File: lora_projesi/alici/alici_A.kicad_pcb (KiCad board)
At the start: 4 copper layers, 88 x 102 mm, 135 parts, among them J1 USB-C, J2 SMA, J3 RJ45, J4 u.FL (ANA ANTEN), J5 12 V GIRIS, J6 LAMBA, J7 MICRO-SIM, K1 SRD-12VDC-SL-A, Q1 AO3401A, Q2 MMBT2222A, Q3 MMBT2222A, Q4 MMBT2222A, SW1 DUGME, U1 ESP32-S3-WROOM-1-N4, U10 A7670SA, U11 AP2112K-3.3, U12 USBLC6-2SC6, U13 USBLC6-2SC6, U14 USBLC6-2SC6, U15 LM66100, U4 Ra-01H, U5 TPS62933DRLR, U6 TPS62933DRLR, U7 USBLC6-2SC6, U8 TXB0104PW, U9 W5500, Y1 25 MHz

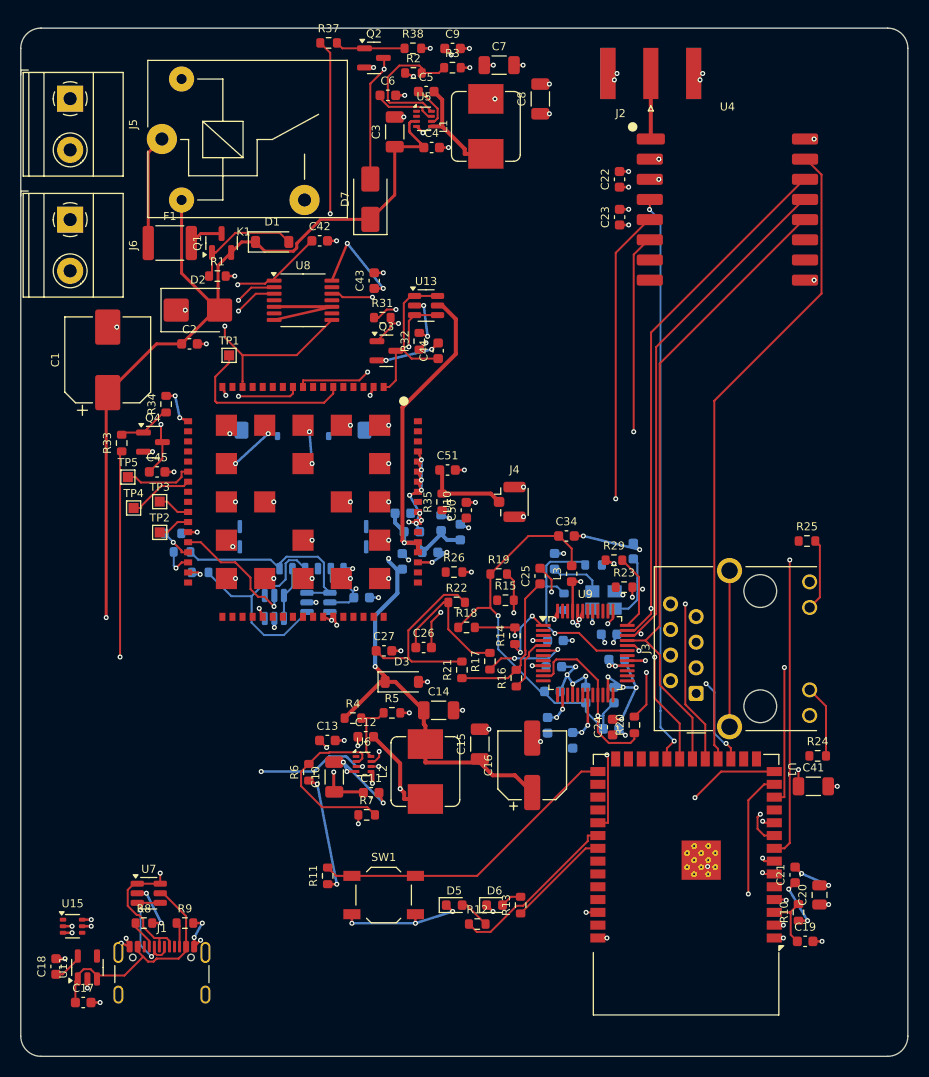
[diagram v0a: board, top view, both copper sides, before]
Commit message: alici_A: izgara onarim dongusu sonrasi kart (2 baglantisiz kaldi)
Co-Authored-By: Claude Sonnet 5.5 <noreply@anthropic.com>
Claude-Session: https://claude.ai/code/session_01Q71gHQtKJ86ZE2CtYTYSwP
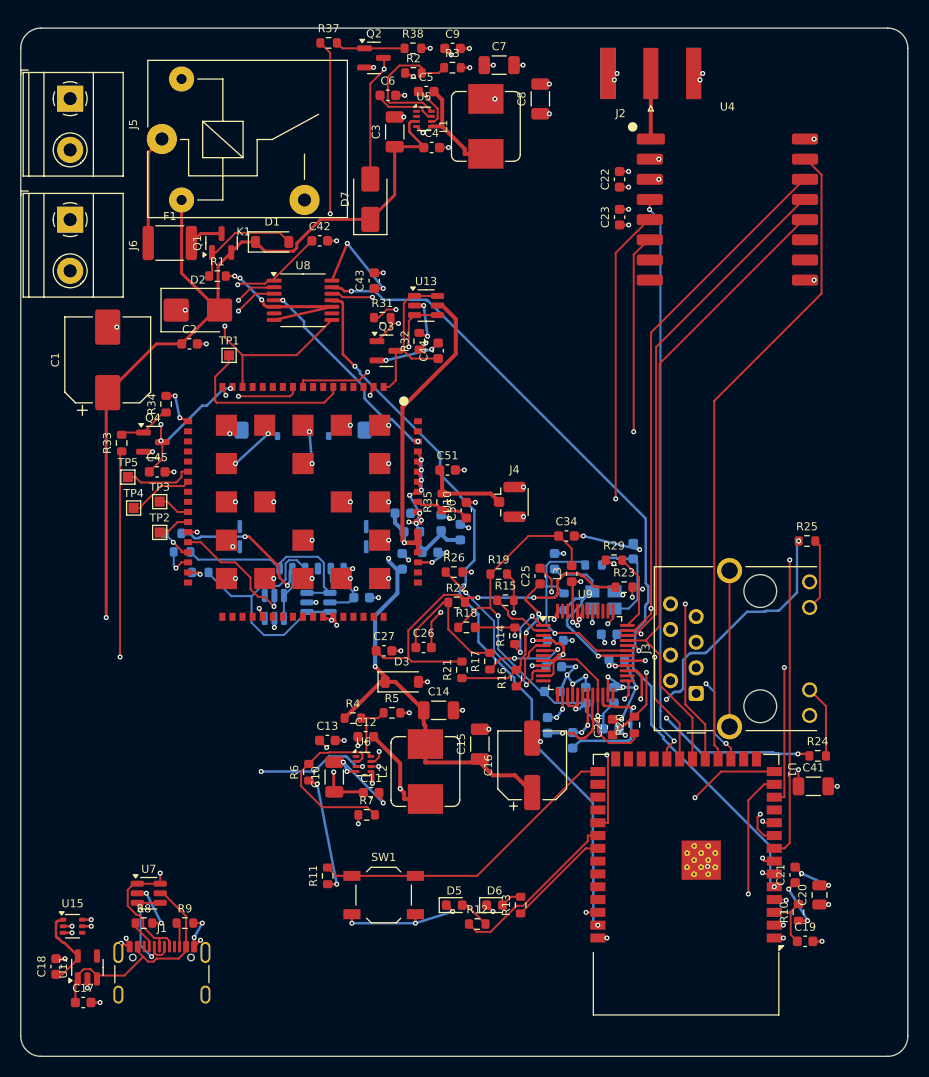
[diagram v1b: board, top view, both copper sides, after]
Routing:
- net MODEM_RXD_H: track 0.00 -> 83.7 mm, vias 0 -> 2
- net MODEM_STATUS: track 0.00 -> 74.6 mm, vias 0 -> 2
- net W_ACTLED: track 0.00 -> 30.7 mm, vias 0 -> 3
- net W_LINKLED: track 0.00 -> 23.2 mm, vias 0 -> 3
- net M_STATUS: track 0.00 -> 21.0 mm, vias 0 -> 2
- net RX_M: track 19.1 -> 37.3 mm, vias 0 -> 2
- net EXRES1: track 0.00 -> 17.1 mm, vias 0 -> 2
- net USIM_DATA: track 5.29 -> 20.6 mm, vias 0 -> 2
- net +3V3A: track 61.5 -> 76.7 mm, vias 3 -> 6
- net XI: track 5.30 -> 19.5 mm, vias 0 -> 1
- net 1V2O: track 0.00 -> 13.5 mm, vias 0 -> 1
- net MODEM_RESET: track 38.7 -> 48.1 mm, vias 2 -> 4
- net TOCAP: track 0.00 -> 8.60 mm, vias 0 -> 1
- net W_TXP: track 0.00 -> 6.05 mm
- net MODEM_ANT: track 0.00 -> 5.49 mm
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
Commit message: alici_A: J3 pin 9 +3V3 via ve iz
Co-Authored-By: Claude Sonnet 5.5 <noreply@anthropic.com>
Claude-Session: https://claude.ai/code/session_01Q71gHQtKJ86ZE2CtYTYSwP
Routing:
- net +3V3: track 51.1 -> 53.5 mm, vias 26 -> 27
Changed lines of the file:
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@@
   (via (at 35.9625 25.825) (size 0.5) (drill 0.25) (layers "F.Cu" "B.Cu") (net 2))
   (via (at 5.090105 89.744566) (size 0.5) (drill 0.25) (layers "F.Cu" "B.Cu") (net 2))
+  (via (at 80.6 68.19) (size 0.5) (drill 0.25) (layers "F.Cu" "B.Cu") (net 2))
   (via (at 78.05 88.545) (size 0.5) (drill 0.25) (layers "F.Cu" "B.Cu") (net 2))
   (via (at 55.405584 58.668991) (size 0.5) (drill 0.25) (layers "F.Cu" "B.Cu") (net 2))
@@
   (segment (start 55.25 59.2375) (end 54.75 58.9375) (width 0.25) (layer "B.Cu") (net 2))
   (segment (start 58.348269 62.65) (end 58.984665 63.286396) (width 0.25) (layer "B.Cu") (net 2))
+  (segment (start 78.26 68.185) (end 80.6 68.19) (width 0.25) (layer "B.Cu") (net 2))
   (segment (start 76.180093 85.412446) (end 78.05 88.545) (width 0.25) (layer "B.Cu") (net 2))
   (segment (start 32.393233 21.354481) (end 35.9625 25.825) (width 0.25) (layer "B.Cu") (net 2))

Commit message: alici_A: +3V3 ada koprusu via
Co-Authored-By: Claude Sonnet 5.5 <noreply@anthropic.com>
Claude-Session: https://claude.ai/code/session_01Q71gHQtKJ86ZE2CtYTYSwP
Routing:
- net +3V3: track 53.5 -> 61.0 mm, vias 27 -> 28
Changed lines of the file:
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@@
   (segment (start 62.4 15) (end 63.3 15) (width 0.25) (layer "F.Cu") (net 2))
   (segment (start 59.407248 19.527791) (end 60.307248 19.527791) (width 0.25) (layer "F.Cu") (net 2))
+  (segment (start 58.85 53.13) (end 57.547638 45.743941) (width 0.25) (layer "F.Cu") (net 2))
   (segment (start 79.239935 86.93992) (end 80.139935 86.93992) (width 0.25) (layer "F.Cu") (net 2))
   (segment (start 76.81649 84.77605) (end 76.180093 85.412446) (width 0.25) (layer "F.Cu") (net 2))
@@
   (via (at 60.307248 19.527791) (size 0.5) (drill 0.25) (layers "F.Cu" "B.Cu") (net 2))
   (via (at 58.984665 63.286396) (size 0.5) (drill 0.25) (layers "F.Cu" "B.Cu") (net 2))
+  (via (at 57.547638 45.743941) (size 0.5) (drill 0.25) (layers "F.Cu" "B.Cu") (net 2))
   (via (at 35.9625 25.825) (size 0.5) (drill 0.25) (layers "F.Cu" "B.Cu") (net 2))
   (via (at 5.090105 89.744566) (size 0.5) (drill 0.25) (layers "F.Cu" "B.Cu") (net 2))
